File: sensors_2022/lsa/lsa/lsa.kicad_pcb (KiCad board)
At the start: 2 copper layers, 61.7 x 22.7 mm, 31 parts, among them J1 Conn_01x06_Male, U1 LM324

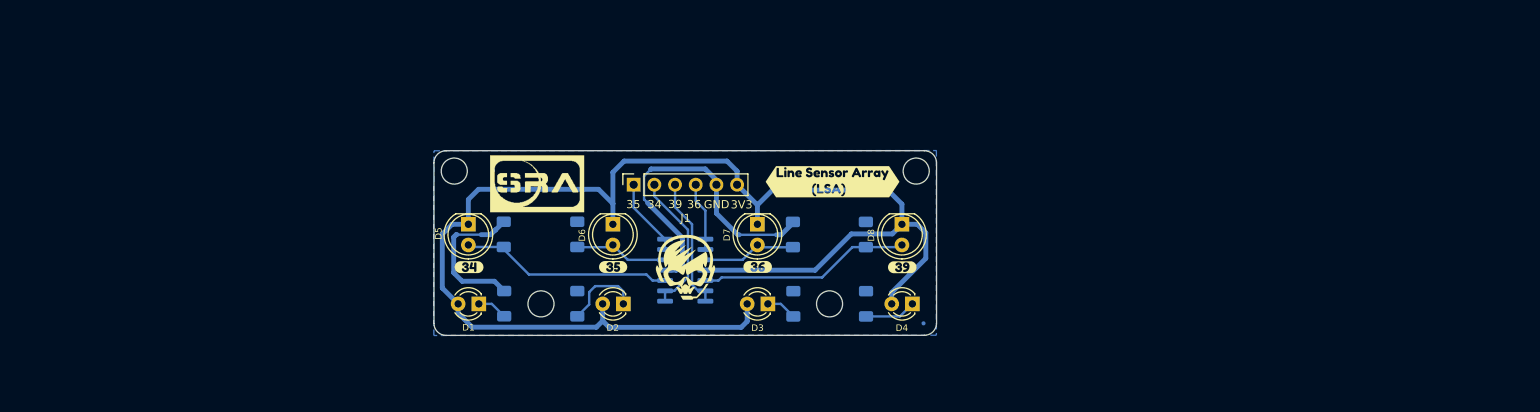
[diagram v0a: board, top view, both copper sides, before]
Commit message: add TCRT-5000 base structure to LSA
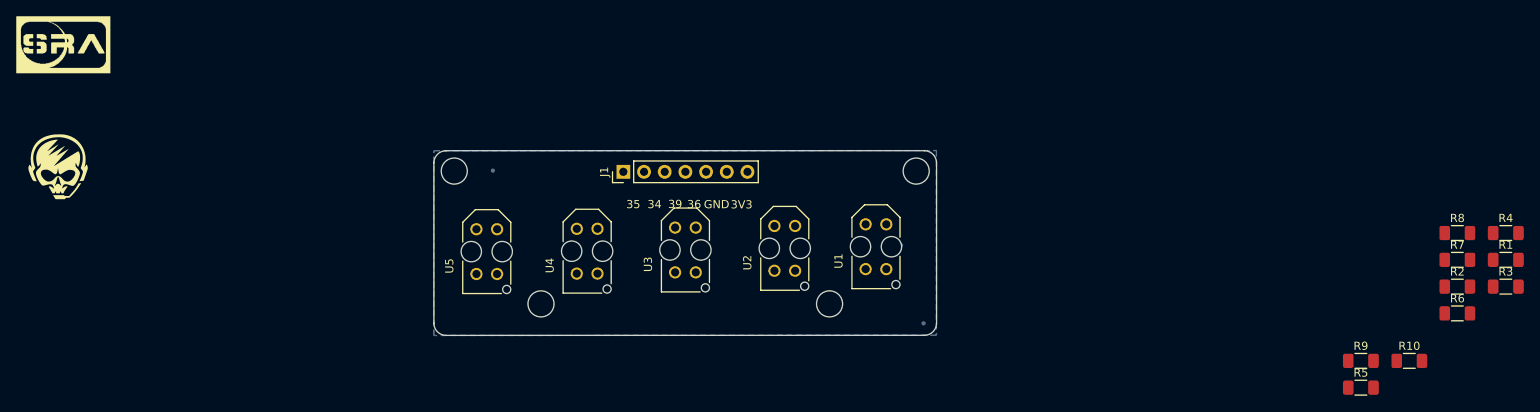
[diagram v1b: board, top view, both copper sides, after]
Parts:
- removed D1, D2, D3, D4: LED, LED_THT:LED_D3.0mm
- removed D5, D6, D7, D8: D_Photo, LED_THT:LED_D5.0mm
- removed kibuzzard-61F951E2: G***, kibuzzard-61F951E2
- removed kibuzzard-61F951FA: G***, kibuzzard-61F951FA
- removed kibuzzard-61F95211: G***, kibuzzard-61F95211
- removed kibuzzard-61F95227: G***, kibuzzard-61F95227
- removed kibuzzard-61F9742D: G***, kibuzzard-61F9742D
- added R10: 4.7k, Resistor_SMD:R_1206_3216Metric_Pad1.30x1.75mm_HandSolder, F.Cu at (205.1, 95.2)
- added R9: 150E, Resistor_SMD:R_1206_3216Metric_Pad1.30x1.75mm_HandSolder, F.Cu at (199.2, 95.2)
- added U2: TCRT5000, TCRT5000:OPTO_TCRT5000, F.Cu at (128.4, 81.4)
- added U3: TCRT5000, TCRT5000:OPTO_TCRT5000, F.Cu at (116.2, 81.6)
- added U4: TCRT5000, TCRT5000:OPTO_TCRT5000, F.Cu at (104.1, 81.8)
- added U5: TCRT5000, TCRT5000:OPTO_TCRT5000, F.Cu at (91.8, 81.8)
- J1: value Conn_01x06_Male -> Conn_01x07_Male; footprint Connector_PinSocket_2.54mm:PinSocket_1x06_P2.54mm_Vertical -> Connector_PinHeader_2.54mm:PinHeader_1x07_P2.54mm_Vertical
- R1, R3: value 75 -> 150E; moved to F.Cu
- R2, R4: value 75 -> 4.7k; moved to F.Cu
- R5, R7: value 10k -> 150E; moved to F.Cu
- R6, R8: value 10k -> 4.7k; moved to F.Cu
- U1: value LM324 -> TCRT5000; footprint Package_SO:SOIC-14_3.9x8.7mm_P1.27mm -> TCRT5000:OPTO_TCRT5000; moved to F.Cu
- moved R1 123.1 mm to (216.9, 82.8), turned to 0 degrees
- moved R6 108.5 mm to (211.0, 89.4), turned to 0 degrees
- moved R2 108.1 mm to (211.0, 86.1), turned to 0 degrees
- moved R5 106.9 mm to (199.2, 98.5), turned to 0 degrees
- moved R3 87.5 mm to (216.9, 86.1), turned to 0 degrees
- moved R7 81.7 mm to (211.0, 82.8), turned to 0 degrees
- moved R4 79.0 mm to (216.9, 79.5), turned to 0 degrees
- moved G*** 78.0 mm to (39.2, 71.4)
- moved R8 72.6 mm to (211.0, 79.5), turned to 0 degrees
- moved G*** 60.6 mm to (39.8, 56.4)
- moved U1 23.6 mm to (139.6, 81.2), turned to 90 degrees
- moved J1 2.03 mm to (108.6, 72.0)
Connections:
- J1 pad 1: /A3_35 -> /A4_32
- J1 pad 2: /A2_34 -> /A3_35
- J1 pad 3: /A1_39 -> /A2_34
- J1 pad 4: /A0_36 -> /A1_39
- J1 pad 5: GND -> /A0_36
- J1 pad 6: +3V3 -> GND
- R1 pad 1: Net-(D1-Pad1) -> +3V3
- R1 pad 2: GND -> Net-(R1-Pad2)
- R2 pad 1: Net-(D2-Pad1) -> /A0_36
- R2 pad 2: GND -> +3V3
- R3 pad 1: Net-(D3-Pad1) -> +3V3
- R3 pad 2: GND -> Net-(R3-Pad2)
- R4 pad 1: Net-(D4-Pad1) -> /A1_39
- R4 pad 2: GND -> +3V3
- R5 pad 1: /LSA_A2 -> +3V3
- R5 pad 2: GND -> Net-(R5-Pad2)
- R6 pad 1: /LSA_A3 -> /A2_34
- R6 pad 2: GND -> +3V3
- R7 pad 1: /LSA_A0 -> +3V3
- R7 pad 2: GND -> Net-(R7-Pad2)
- R8 pad 1: /LSA_A1 -> /A3_35
- R8 pad 2: GND -> +3V3
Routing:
- net +3V3: track 169.9 -> 0.00 mm
- net GND: track 59.0 -> 0.00 mm
- net /LSA_A1: track 26.4 -> 0.00 mm
- net /LSA_A2: track 26.1 -> 0.00 mm
- net /A2_34: track 17.8 -> 0.00 mm
- net /A1_39: track 16.4 -> 0.00 mm
- net /LSA_A3: track 11.7 -> 0.00 mm
- net /LSA_A0: track 11.6 -> 0.00 mm
- net Net-(D2-Pad1): track 9.88 -> 0.00 mm
- net /A3_35: track 9.55 -> 0.00 mm
- net /A0_36: track 8.45 -> 0.00 mm
- net Net-(D4-Pad1): track 6.33 -> 0.00 mm
- net Net-(D3-Pad1): track 3.76 -> 0.00 mm
- net Net-(D1-Pad1): track 3.74 -> 0.00 mm
- net (no net): track 0.00 -> 0.85 mm
